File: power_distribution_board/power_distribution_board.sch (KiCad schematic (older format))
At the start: 13 parts

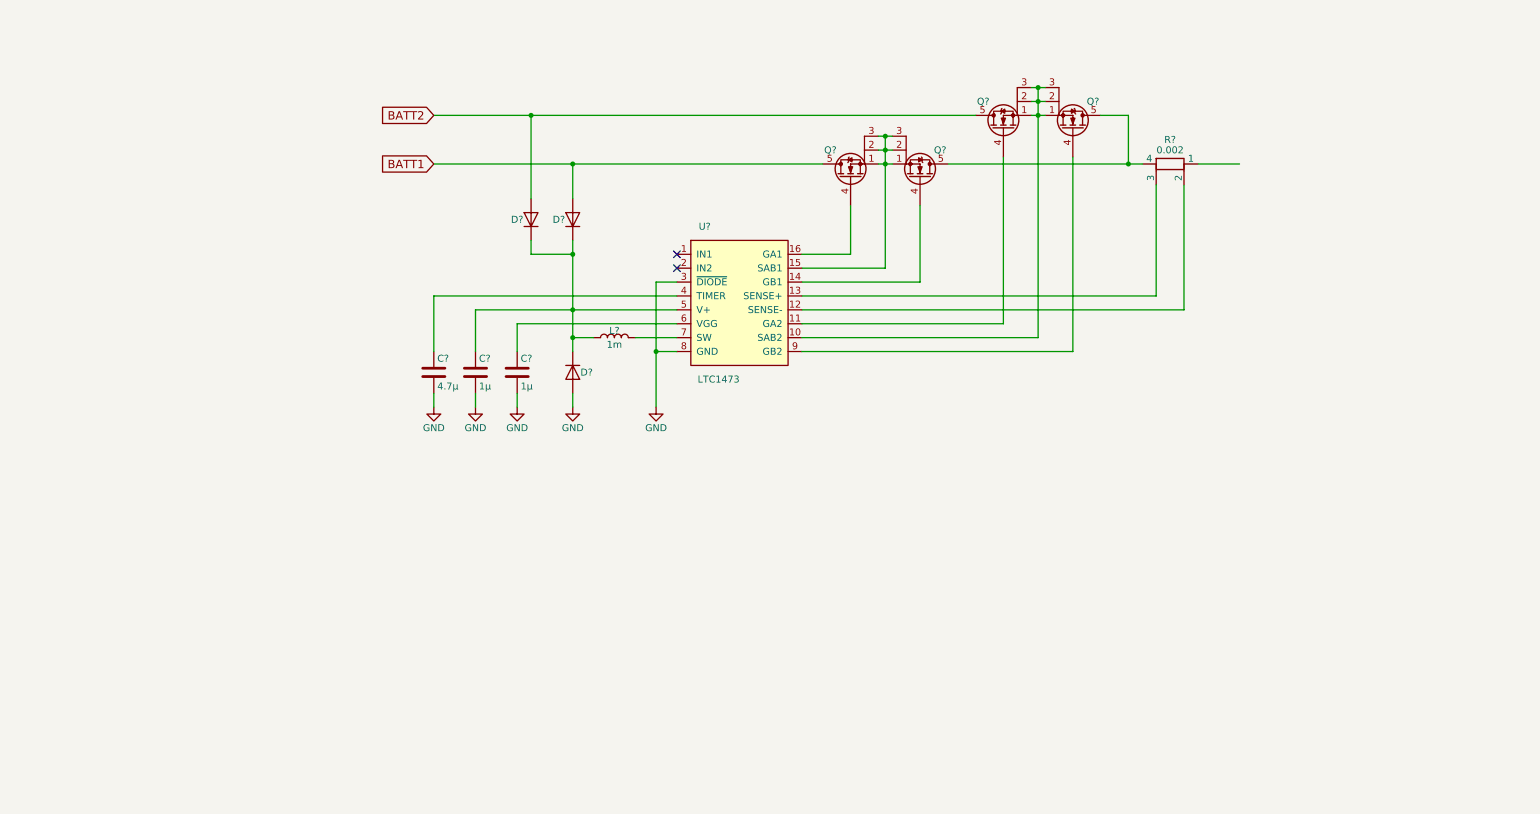
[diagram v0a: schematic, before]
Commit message: add header to debug battery switch control
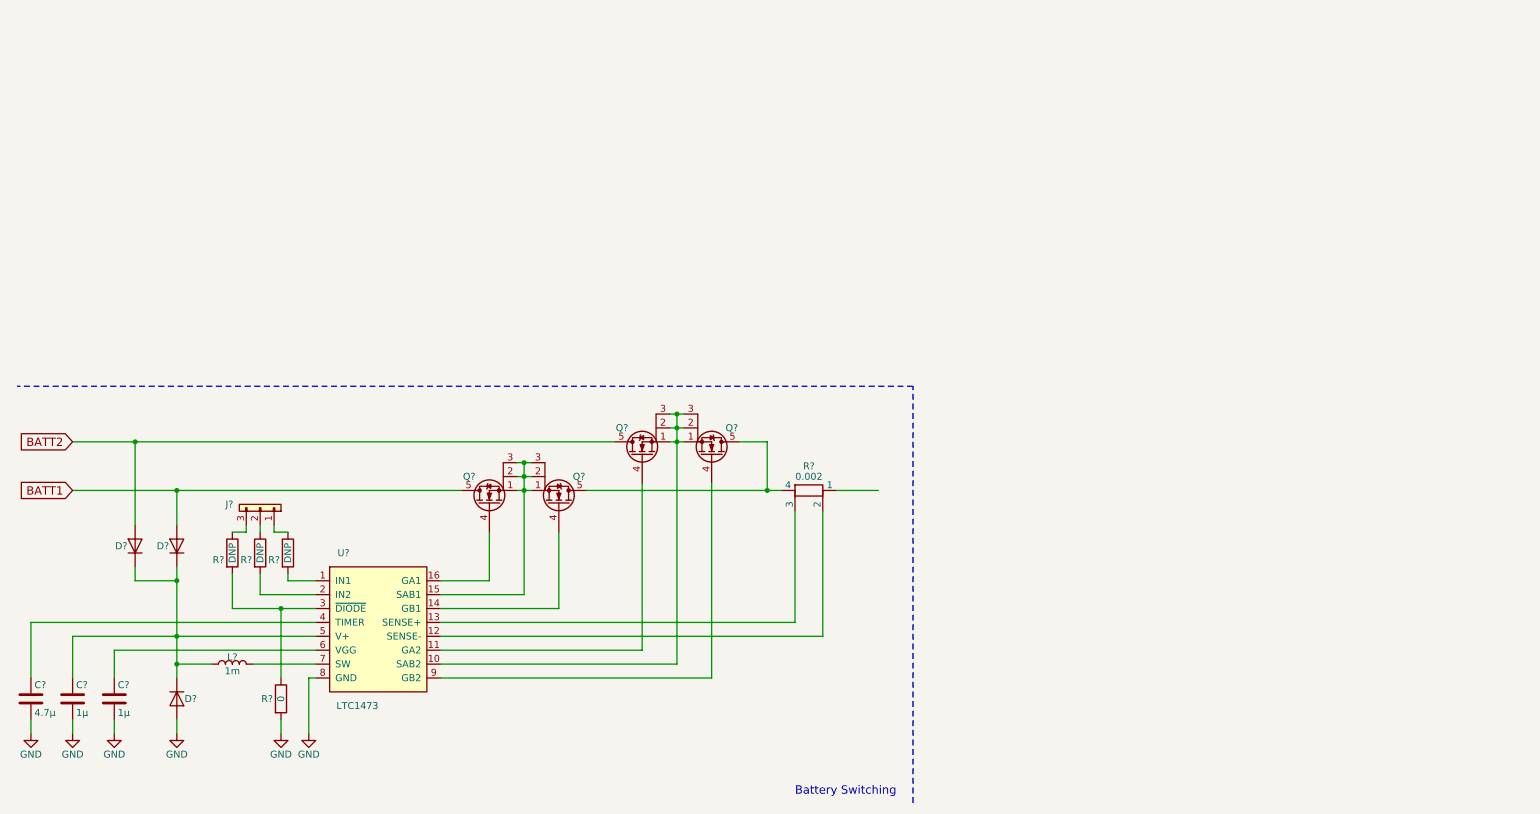
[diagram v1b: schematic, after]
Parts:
- added J?: CONN_01x03, symbol CONN_01x03
- added R? (x3): DNP, symbol R
- added R?: 0, symbol R
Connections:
- net GND: now also R?.2; no longer U?.3 (~DIODE)
- net at U?.1 (IN1): now also R?.2
- net at U?.2 (IN2): now also R?.2
- new net: R?.1, R?.2, U?.3 (~DIODE)
- new net: J?.2, R?.1
- new net: J?.1, R?.1
- new net: J?.3, R?.1
- no-connect marks 2 -> 0
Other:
- note added: "Battery Switching"
- moved on the sheet: C?, D?, L?, Q?, R?, U?

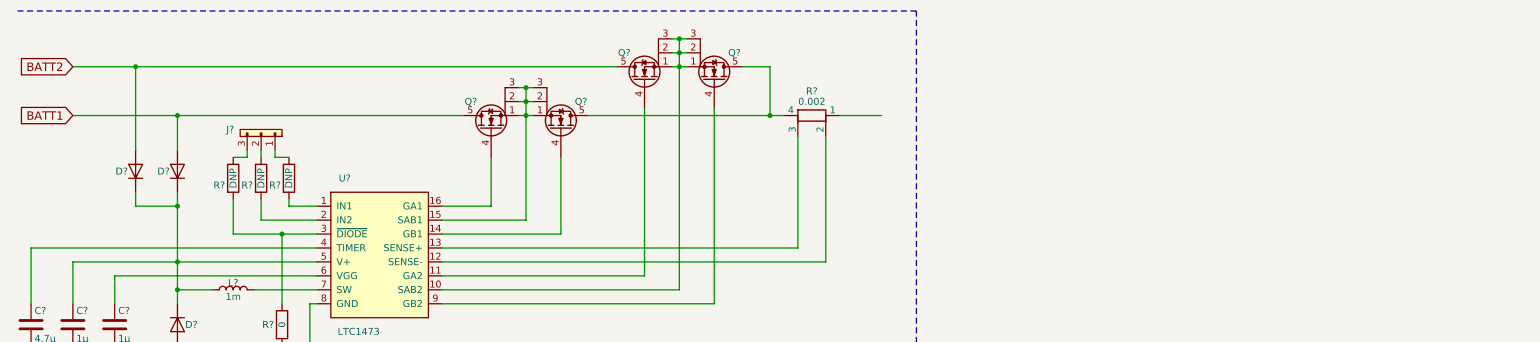
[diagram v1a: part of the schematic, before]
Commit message: add hall effect killswitch
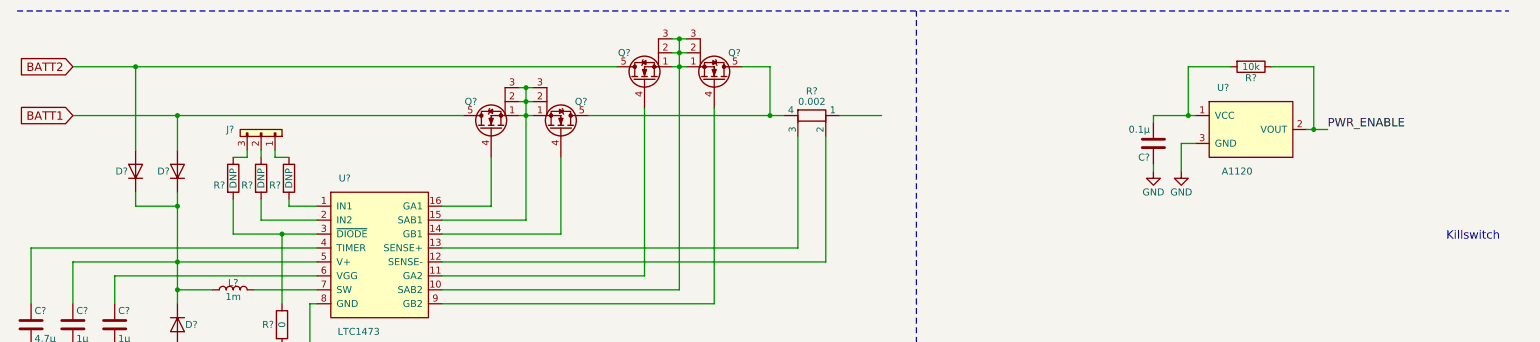
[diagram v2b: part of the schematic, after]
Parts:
- added C?: 0.1μ, symbol C
- added R?: 10k, symbol R
- added U?: A1120, symbol A1120
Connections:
- net GND: now also C?.1, U?.3 (GND)
- new net: C?.2, R?.2, U?.1 (VCC)
- new net PWR_ENABLE: R?.1, U?.2 (VOUT)
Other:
- note added: "Killswitch"
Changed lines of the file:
@@
 	6950 7800 6950 4800
 Wire Notes Line
-	6950 4800 500  4800
+	500  4800 11200 4800
 Text Notes 6100 7750 0    60   ~ 0
 Battery Switching
@@
 Wire Wire Line
 	2250 5850 2250 5800
+$Comp
+L A1120 U?
+U 1 1 597E8118
+P 9350 5650
+F 0 "U?" H 9150 5950 50  0000 C CNN
+F 1 "A1120" H 9250 5350 50  0000 C CNN
+F 2 "" H 9250 5650 50  0001 C CNN
+F 3 "" H 9250 5650 50  0001 C CNN
+	1    9350 5650
+	1    0    0    -1
+$EndComp
+$Comp
+L R R?
+U 1 1 597E88C6
+P 9350 5200
+F 0 "R?" V 9430 5200 50  0000 C CNN
+F 1 "10k" V 9350 5200 50  0000 C CNN
+F 2 "" V 9280 5200 50  0001 C CNN
+F 3 "" H 9350 5200 50  0001 C CNN
+	1    9350 5200
+	0    1    1    0
+$EndComp
+Wire Wire Line
+	8650 5550 8950 5550
+Wire Wire Line
+	8900 5550 8900 5200
+Wire Wire Line
+	8900 5200 9200 5200
+Connection ~ 8900 5550
+Wire Wire Line
+	9500 5200 9800 5200
+Wire Wire Line
+	9800 5200 9800 5650
+Wire Wire Line
+	9750 5650 9900 5650
+$Comp
+L GND #PWR?
+U 1 1 597E90C0
+P 8850 5950
+F 0 "#PWR?" H 8850 5700 50  0001 C CNN
+F 1 "GND" H 8850 5800 50  0000 C CNN
+F 2 "" H 8850 5950 50  0001 C CNN
+F 3 "" H 8850 5950 50  0001 C CNN
+	1    8850 5950
+	1    0    0    -1
+$EndComp
+Wire Wire Line
+	8850 5950 8850 5750
+Wire Wire Line
+	8850 5750 8950 5750
+$Comp
+L C C?
+U 1 1 597E9DE7
+P 8650 5750
+F 0 "C?" H 8675 5850 50  0000 L CNN
+F 1 "0.1μ" H 8675 5650 50  0000 L CNN
+F 2 "" H 8688 5600 50  0001 C CNN
+F 3 "" H 8650 5750 50  0001 C CNN
+	1    8650 5750
+	-1   0    0    1
+$EndComp
+$Comp
+L GND #PWR?
+U 1 1 597E9E6C
+P 8650 5950
+F 0 "#PWR?" H 8650 5700 50  0001 C CNN
+F 1 "GND" H 8650 5800 50  0000 C CNN
+F 2 "" H 8650 5950 50  0001 C CNN
+F 3 "" H 8650 5950 50  0001 C CNN
+	1    8650 5950
+	1    0    0    -1
+$EndComp
+Wire Wire Line
+	8650 5950 8650 5900
+Wire Wire Line
+	8650 5600 8650 5550
+Connection ~ 9800 5650
+Text Label 9900 5650 0    60   ~ 0
+PWR_ENABLE
+Text Notes 10750 6450 0    60   ~ 0
+Killswitch
 $EndSCHEMATC

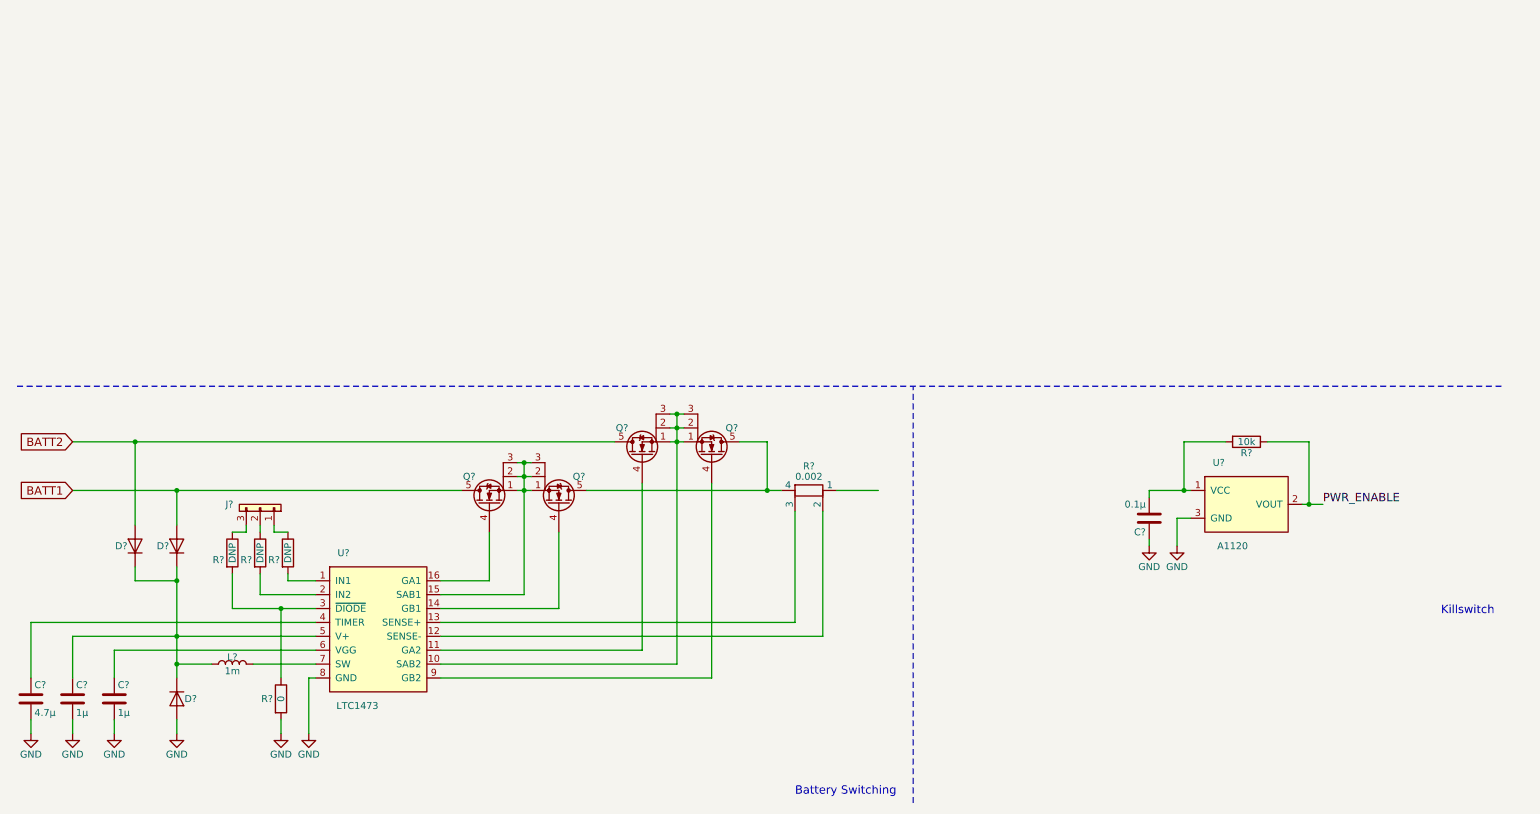
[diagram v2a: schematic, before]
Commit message: add label to battery switch output
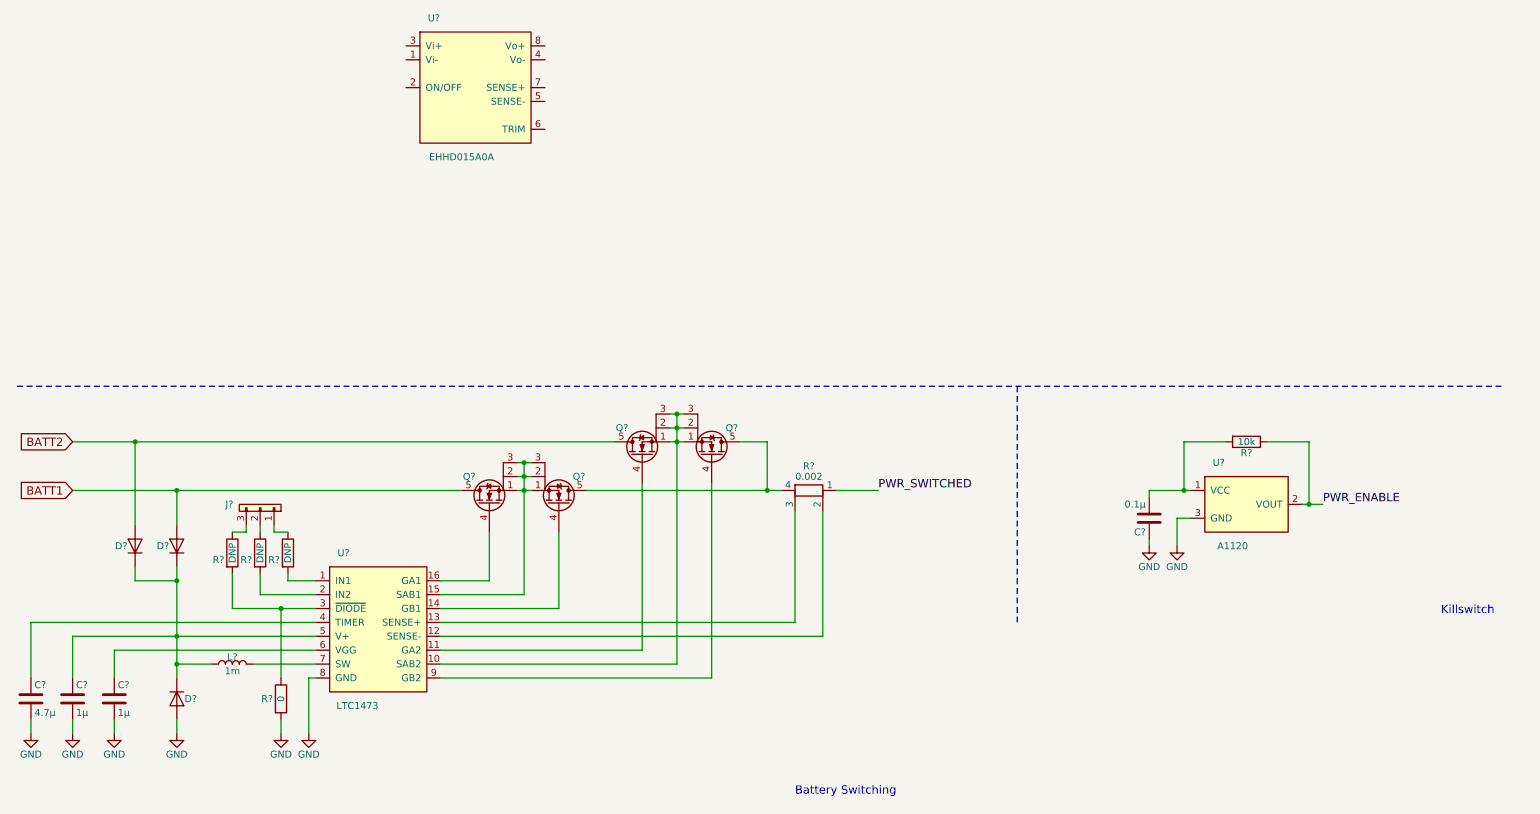
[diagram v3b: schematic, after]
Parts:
- added U?: EHHD015A0A, symbol EHHD015A0A
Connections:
- net PWR_SWITCHED: now reaches R?.1
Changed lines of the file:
@@
 	6400 5550 6700 5550
-Wire Notes Line
-	6950 7800 6950 4800
 Wire Notes Line
 	500  4800 11200 4800
@@
 Text Notes 10750 6450 0    60   ~ 0
 Killswitch
+$Comp
+L EHHD015A0A U?
+U 1 1 597F4834
+P 3800 2650
+F 0 "U?" H 3500 3150 50  0000 C CNN
+F 1 "EHHD015A0A" H 3700 2150 50  0000 C CNN
+F 2 "" H 3500 2600 50  0001 C CNN
+F 3 "" H 3500 2600 50  0001 C CNN
+	1    3800 2650
+	1    0    0    -1
+$EndComp
+Text Label 6700 5550 0    60   ~ 0
+PWR_SWITCHED
+Wire Notes Line
+	7700 4800 7700 6500
 $EndSCHEMATC
